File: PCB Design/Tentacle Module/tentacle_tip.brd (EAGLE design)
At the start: 45.7 x 15.2 mm, 8 parts, among them U1 ADXL345

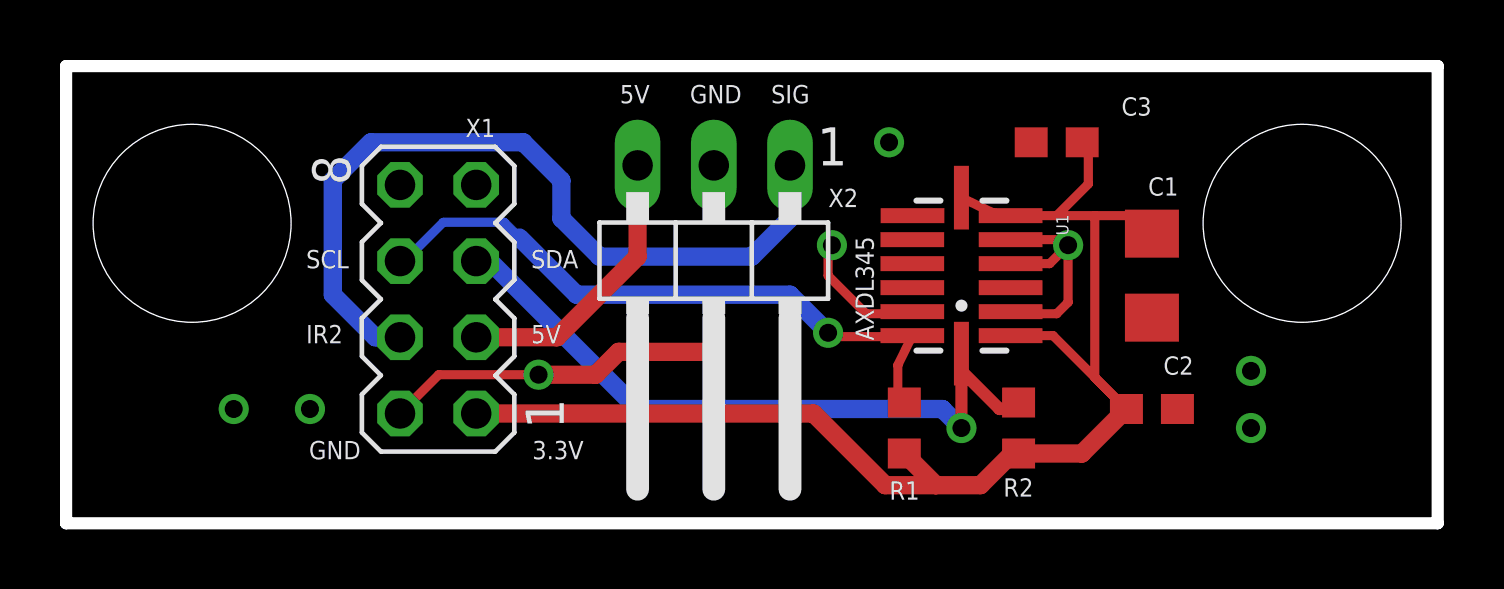
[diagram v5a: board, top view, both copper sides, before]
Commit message: Added labels to silkscreen
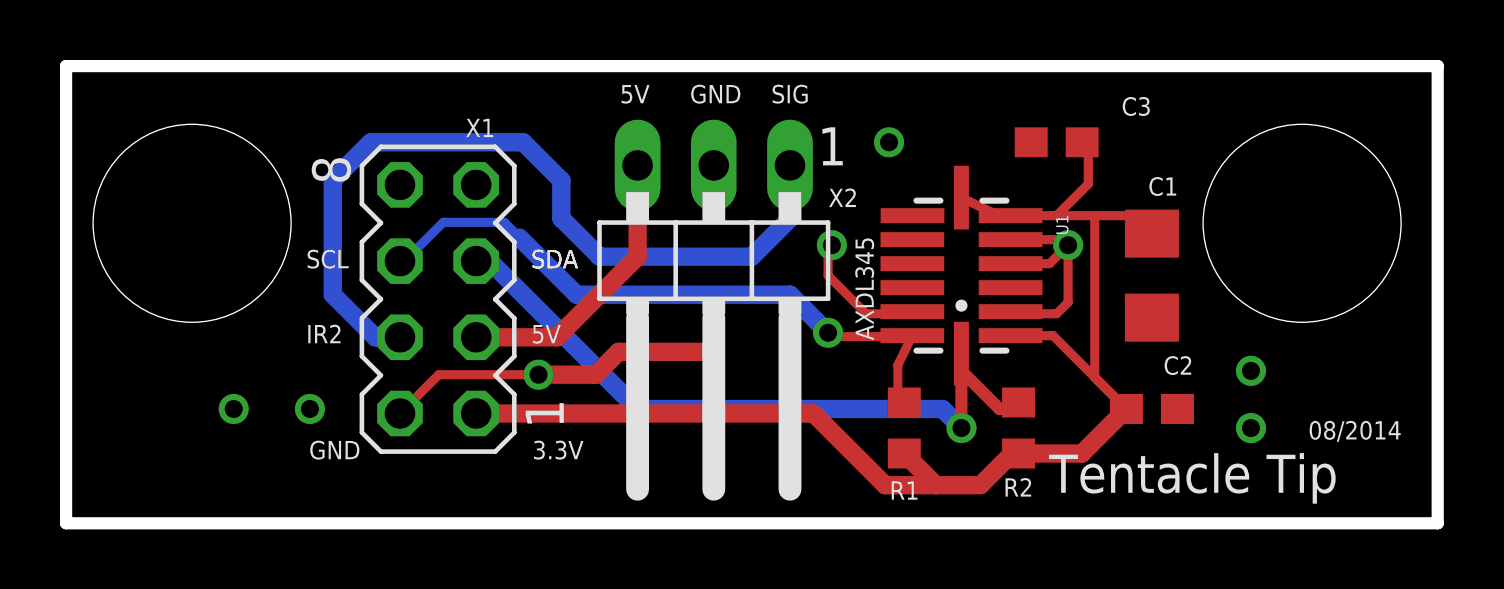
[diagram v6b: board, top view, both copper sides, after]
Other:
- board text added: "08/2014"
- board text added: "Tentacle Tip"
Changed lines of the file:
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@@
 <text x="20.794" y="14" size="0.6096" layer="21">GND</text>
 <text x="26.924" y="6.096" size="0.6096" layer="21" rot="R90">AXDL345</text>
+<text x="9.272" y="8.5" size="0.6096" layer="22" rot="MR0">SCL</text>
+<text x="9.272" y="6" size="0.6096" layer="22" rot="MR0">IR2</text>
+<text x="9.685" y="2.135" size="0.6096" layer="22" rot="MR0">GND</text>
+<text x="17.226" y="2.135" size="0.6096" layer="22" rot="MR0">3.3V</text>
+<text x="16.504" y="6" size="0.6096" layer="22" rot="MR0">5V</text>
+<text x="15.5" y="8.5" size="0.6096" layer="21">SDA</text>
+<text x="17.012" y="8.5" size="0.6096" layer="22" rot="MR0">SDA</text>
+<text x="19.386" y="14" size="0.6096" layer="22" rot="MR0">5V</text>
+<text x="22.386" y="14" size="0.6096" layer="22" rot="MR0">GND</text>
+<text x="24.76" y="14" size="0.6096" layer="22" rot="MR0">SIG</text>
+<text x="32.766" y="1.016" size="1.27" layer="21" ratio="15">Tentacle Tip</text>
+<text x="31.75" y="7.366" size="1.27" layer="22" ratio="15" rot="MR0">Tentacle Tip</text>
+<text x="31.496" y="6.096" size="0.6096" layer="22" ratio="15" rot="MR0">08/2014</text>
+<text x="41.402" y="2.794" size="0.6096" layer="21" ratio="15">08/2014</text>
 </plain>
 <attributes>

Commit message: Generated gerber files
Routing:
- net +3.3V: track 46.6 -> 45.4 mm
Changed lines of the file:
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@@
 </class>
 </classes>
-<designrules name="default *">
-<description language="de">&lt;b&gt;EAGLE Design Rules&lt;/b&gt;
-&lt;p&gt;
-Die Standard-Design-Rules sind so gewählt, dass sie für
-die meisten Anwendungen passen. Sollte ihre Platine
-besondere Anforderungen haben, treffen Sie die erforderlichen
-Einstellungen hier und speichern die Design Rules unter
-einem neuen Namen ab.</description>
+<designrules name="SparkFun">
 <description language="en">&lt;b&gt;EAGLE Design Rules&lt;/b&gt;
 &lt;p&gt;
@@
 <param name="mdViaViaSameLayer" value="8mil"/>
 <param name="mnLayersViaInSmd" value="2"/>
-<param name="mdCopperDimension" value="24mil"/>
+<param name="mdCopperDimension" value="10mil"/>
 <param name="mdDrill" value="8mil"/>
 <param name="mdSmdStop" value="0mil"/>
-<param name="msWidth" value="10mil"/>
+<param name="msWidth" value="8mil"/>
 <param name="msDrill" value="20mil"/>
 <param name="msMicroVia" value="9.99mm"/>
@@
 <param name="rvMicroViaOuter" value="0.25"/>
 <param name="rvMicroViaInner" value="0.25"/>
-<param name="rlMinPadTop" value="10mil"/>
+<param name="rlMinPadTop" value="12mil"/>
 <param name="rlMaxPadTop" value="20mil"/>
 <param name="rlMinPadInner" value="10mil"/>
 <param name="rlMaxPadInner" value="20mil"/>
-<param name="rlMinPadBottom" value="10mil"/>
+<param name="rlMinPadBottom" value="12mil"/>
 <param name="rlMaxPadBottom" value="20mil"/>
-<param name="rlMinViaOuter" value="8mil"/>
+<param name="rlMinViaOuter" value="10mil"/>
 <param name="rlMaxViaOuter" value="20mil"/>
-<param name="rlMinViaInner" value="8mil"/>
+<param name="rlMinViaInner" value="10mil"/>
 <param name="rlMaxViaInner" value="20mil"/>
 <param name="rlMinMicroViaOuter" value="4mil"/>
@@
 <param name="mlMinCreamFrame" value="0mil"/>
 <param name="mlMaxCreamFrame" value="0mil"/>
-<param name="mlViaStopLimit" value="0mil"/>
+<param name="mlViaStopLimit" value="25mil"/>
 <param name="srRoundness" value="0"/>
 <param name="srMinRoundness" value="0mil"/>
@@
 <wire x1="34.075" y1="12.495" x2="33.87" y2="12.7" width="0.3048" layer="1"/>
 <wire x1="31.4831" y1="10.255" x2="33.02" y2="10.255" width="0.3048" layer="1"/>
-<wire x1="33.02" y1="10.255" x2="34.29" y2="10.255" width="0.3048" layer="1"/>
-<wire x1="34.29" y1="10.255" x2="35.465" y2="10.255" width="0.3048" layer="1"/>
+<wire x1="33.02" y1="10.255" x2="34.544" y2="10.255" width="0.3048" layer="1"/>
+<wire x1="34.544" y1="10.255" x2="35.465" y2="10.255" width="0.3048" layer="1"/>
 <wire x1="35.465" y1="10.255" x2="35.56" y2="10.16" width="0.3048" layer="1"/>
 <wire x1="35.56" y1="10.16" x2="36.195" y2="9.655" width="0.3048" layer="1"/>
 <wire x1="31.75" y1="2.325" x2="33.86" y2="2.325" width="0.6096" layer="1"/>
 <wire x1="33.86" y1="2.325" x2="35.345" y2="3.81" width="0.6096" layer="1"/>
-<wire x1="34.29" y1="10.255" x2="34.29" y2="4.865" width="0.3048" layer="1"/>
-<wire x1="34.29" y1="4.865" x2="35.345" y2="3.81" width="0.3048" layer="1"/>
-<wire x1="32.9" y1="6.255" x2="35.345" y2="3.81" width="0.3048" layer="1"/>
+<wire x1="34.544" y1="10.255" x2="34.544" y2="4.611" width="0.3048" layer="1"/>
+<wire x1="32.9" y1="6.255" x2="34.544" y2="4.611" width="0.3048" layer="1"/>
+<wire x1="34.544" y1="4.611" x2="35.345" y2="3.81" width="0.3048" layer="1"/>
 <wire x1="27.94" y1="2.325" x2="28.995" y2="1.27" width="0.6096" layer="1"/>
 <wire x1="28.995" y1="1.27" x2="30.48" y2="1.27" width="0.6096" layer="1"/>
